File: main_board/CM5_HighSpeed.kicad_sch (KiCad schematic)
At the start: 13 parts, among them J1 USB3_A, J2 USB3_A, J22 690-019-298-412, U12 RT9742SNGV, U6 AP22653W6

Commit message: More power management goodness
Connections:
- net +5v renamed +5V
- net USBOTG_ID: no longer names the net of Module1.101 (USB_OTG_ID)
- no-connect marks 5 -> 35

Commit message: Finalize power management
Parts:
- J1: footprint Library:U3BU1ASMT1 -> 000_custom:U3BU1ASMT1
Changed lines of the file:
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@@
 			)
 		)
-		(property "Footprint" "Library:U3BU1ASMT1"
+		(property "Footprint" "000_custom:U3BU1ASMT1"
 			(at 262.89 40.64 0)
 			(effects

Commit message: Start reouting USB hub
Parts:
- removed J2: USB3_A, Library:U3BU1ASMT1, symbol Connector:USB3_A
- added J8: Conn_01x22_Female, CM5IO:Hirose_FH12-22S-0.5SH_1x22-1MP_P0.50mm_Horizontal, symbol Connector:Conn_01x22_Socket
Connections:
- net USB3-1-D_N renamed USB3_1_DN
- net USB3-1-D_P renamed USB3_1_DP
- net USB3-1-RX_N renamed USB3_1_RX_N
- net USB3-1-RX_P renamed USB3_1_RX_P
- net USB3-1-TX_N renamed USB3_1_TX_N
- net USB3-1-TX_P renamed USB3_1_TX_P

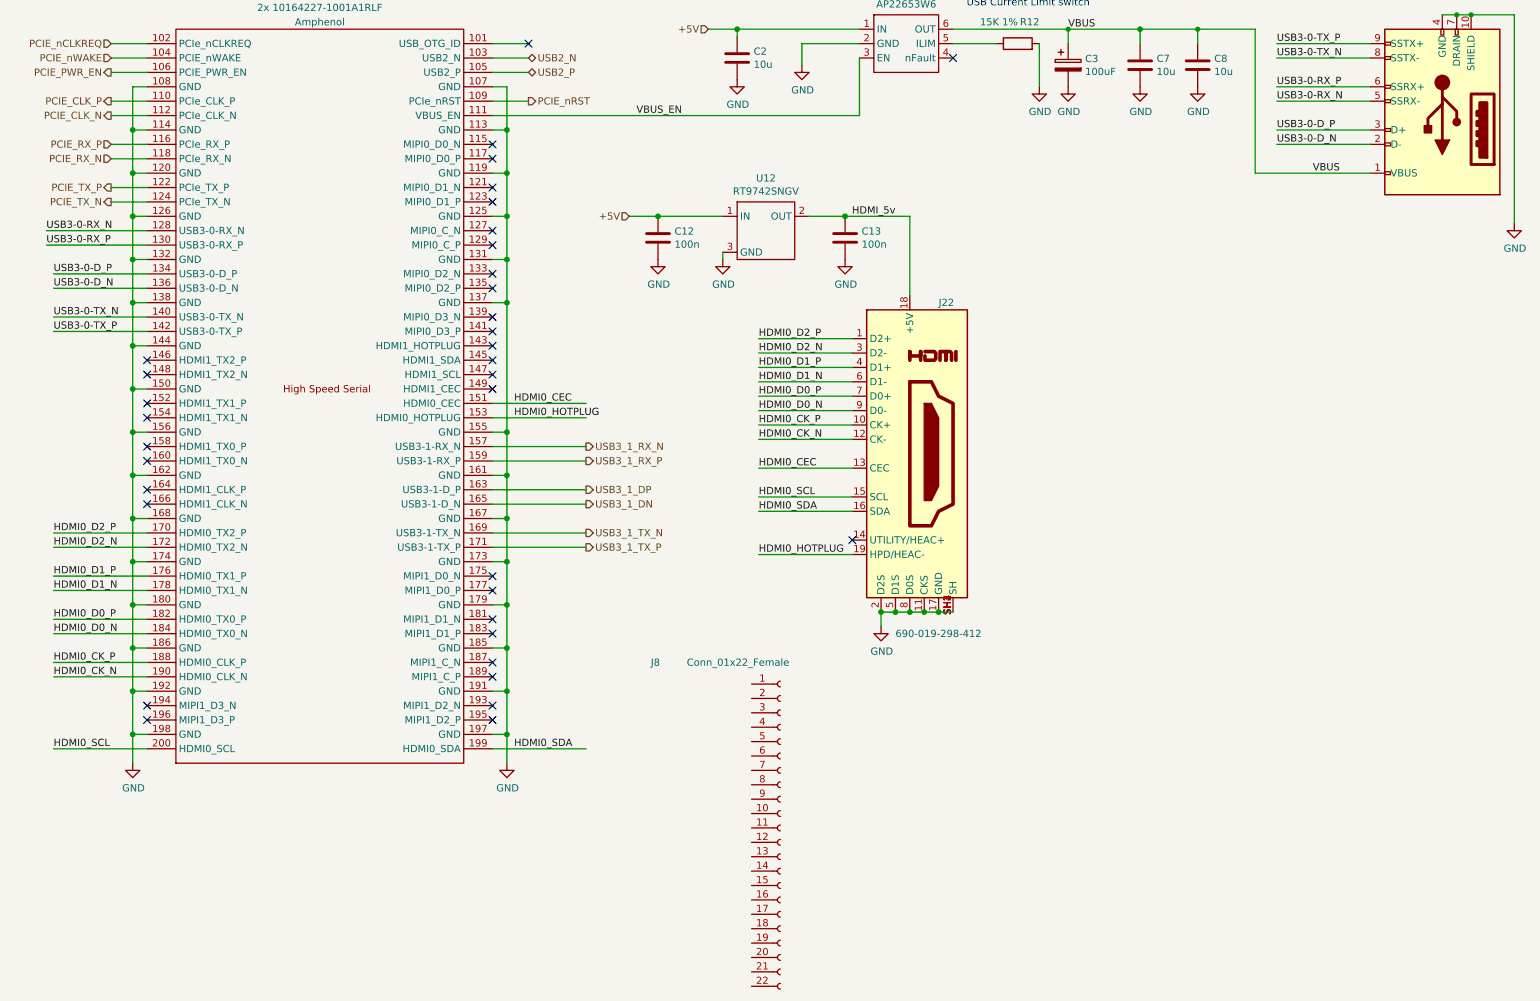
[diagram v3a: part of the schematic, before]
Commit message: Bunch more routing, mainly added MIPI interface, reworked power management a bit
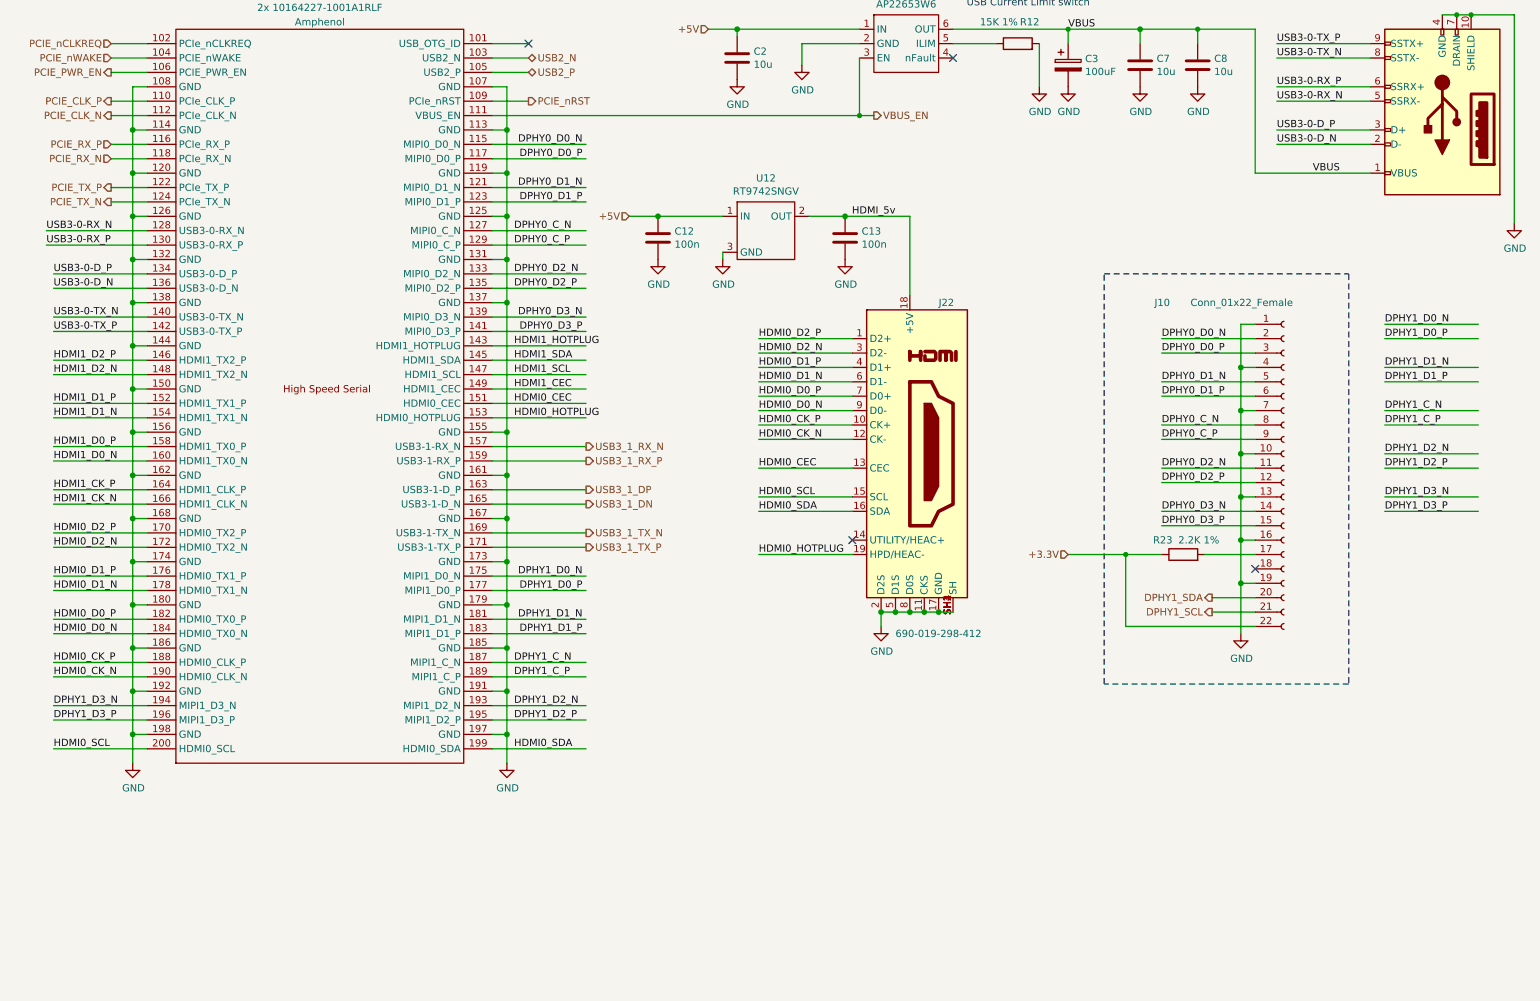
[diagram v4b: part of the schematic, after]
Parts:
- removed J8: Conn_01x22_Female, CM5IO:Hirose_FH12-22S-0.5SH_1x22-1MP_P0.50mm_Horizontal, symbol Connector:Conn_01x22_Socket
- added J10: Conn_01x22_Female, CM5IO:Hirose_FH12-22S-0.5SH_1x22-1MP_P0.50mm_Horizontal, symbol Connector:Conn_01x22_Socket
- added R23: 2.2K 1%, Resistor_SMD:R_0805_2012Metric_Pad1.20x1.40mm_HandSolder, symbol Device:R
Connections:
- net GND: now also J10.1 (Pin_1), J10.10 (Pin_10), J10.13 (Pin_13), J10.16 (Pin_16), J10.19 (Pin_19), J10.4 (Pin_4), J10.7 (Pin_7)
- net DPHY0_D0_N: now reaches Module1.115 (MIPI0_D0_N)
- net DPHY0_D0_N: now also J10.2 (Pin_2)
- net DPHY0_D0_P: now reaches Module1.117 (MIPI0_D0_P)
- net DPHY0_D0_P: now also J10.3 (Pin_3)
- net DPHY0_D1_N: now reaches Module1.121 (MIPI0_D1_N)
- net DPHY0_D1_N: now also J10.5 (Pin_5)
- net DPHY0_D1_P: now reaches Module1.123 (MIPI0_D1_P)
- net DPHY0_D1_P: now also J10.6 (Pin_6)
- net DPHY0_C_N: now reaches Module1.127 (MIPI0_C_N)
- net DPHY0_C_N: now also J10.8 (Pin_8)
- net DPHY0_C_P: now reaches Module1.129 (MIPI0_C_P)
- net DPHY0_C_P: now also J10.9 (Pin_9)
- net DPHY0_D2_N: now reaches Module1.133 (MIPI0_D2_N)
- net DPHY0_D2_N: now also J10.11 (Pin_11)
- net DPHY0_D2_P: now reaches Module1.135 (MIPI0_D2_P)
- net DPHY0_D2_P: now also J10.12 (Pin_12)
- net DPHY0_D3_N: now reaches Module1.139 (MIPI0_D3_N)
- net DPHY0_D3_N: now also J10.14 (Pin_14)
- net DPHY0_D3_P: now reaches Module1.141 (MIPI0_D3_P)
- net DPHY0_D3_P: now also J10.15 (Pin_15)
- net HDMI1_HOTPLUG: now reaches Module1.143 (HDMI1_HOTPLUG)
- net HDMI1_SDA: now reaches Module1.145 (HDMI1_SDA)
- net HDMI1_D2_P: now reaches Module1.146 (HDMI1_TX2_P)
- net HDMI1_SCL: now reaches Module1.147 (HDMI1_SCL)
- net HDMI1_D2_N: now reaches Module1.148 (HDMI1_TX2_N)
- net HDMI1_CEC: now reaches Module1.149 (HDMI1_CEC)
- net HDMI1_D1_P: now reaches Module1.152 (HDMI1_TX1_P)
- net HDMI1_D1_N: now reaches Module1.154 (HDMI1_TX1_N)
- net HDMI1_D0_P: now reaches Module1.158 (HDMI1_TX0_P)
- net HDMI1_D0_N: now reaches Module1.160 (HDMI1_TX0_N)
- net HDMI1_CK_P: now reaches Module1.164 (HDMI1_CLK_P)
- net HDMI1_CK_N: now reaches Module1.166 (HDMI1_CLK_N)
- net DPHY1_D0_N: now reaches Module1.175 (MIPI1_D0_N)
- net DPHY1_D0_P: now reaches Module1.177 (MIPI1_D0_P)
- net DPHY1_D1_N: now reaches Module1.181 (MIPI1_D1_N)
- net DPHY1_D1_P: now reaches Module1.183 (MIPI1_D1_P)
- net DPHY1_C_N: now reaches Module1.187 (MIPI1_C_N)
- net DPHY1_C_P: now reaches Module1.189 (MIPI1_C_P)
- net DPHY1_D2_N: now reaches Module1.193 (MIPI1_D2_N)
- net DPHY1_D3_N: now reaches Module1.194 (MIPI1_D3_N)
- net DPHY1_D2_P: now reaches Module1.195 (MIPI1_D2_P)
- net DPHY1_D3_P: now reaches Module1.196 (MIPI1_D3_P)
- new net: J10.17 (Pin_17), R23.2
- new net +3.3V: J10.22 (Pin_22), R23.1
- new net DPHY1_SCL: J10.21 (Pin_21)
- new net DPHY1_SDA: J10.20 (Pin_20)
- no-connect marks 35 -> 4

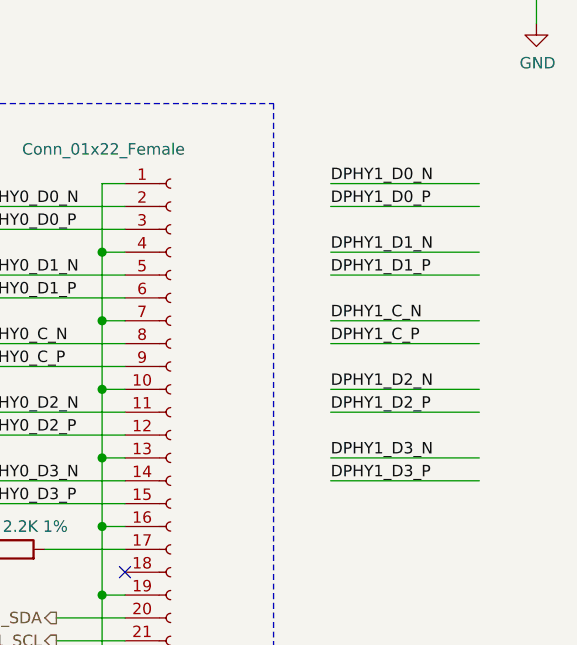
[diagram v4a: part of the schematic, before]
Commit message: Implement power monitoring
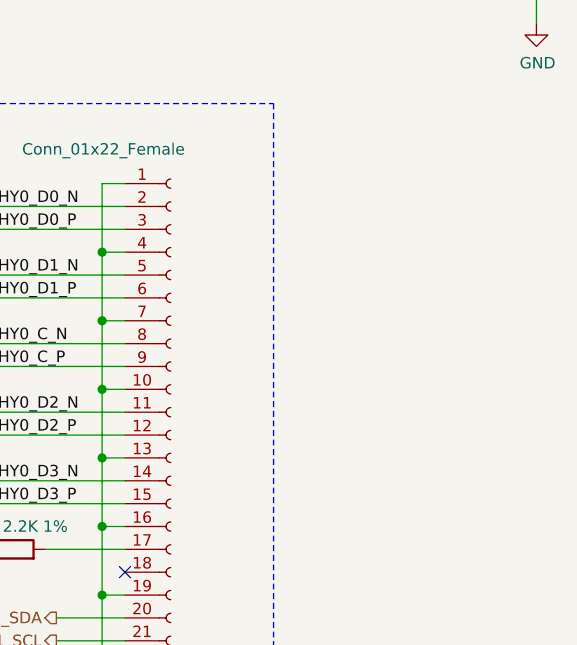
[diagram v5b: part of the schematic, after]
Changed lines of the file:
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@@
-	(wire
-		(pts
-			(xy 256.54 82.55) (xy 273.05 82.55)
-		)
-		(stroke
-			(width 0)
-			(type solid)
-		)
-	)
 	(wire
 		(pts
@@
 	(wire
 		(pts
-			(xy 256.54 92.71) (xy 273.05 92.71)
-		)
-		(stroke
-			(width 0)
-			(type solid)
-		)
-	)
-	(wire
-		(pts
-			(xy 256.54 77.47) (xy 273.05 77.47)
-		)
-		(stroke
-			(width 0)
-			(type solid)
-		)
-	)
-	(wire
-		(pts
 			(xy 99.06 91.44) (xy 115.57 91.44)
 		)
@@
 	(wire
 		(pts
-			(xy 256.54 105.41) (xy 273.05 105.41)
-		)
-		(stroke
-			(width 0)
-			(type solid)
-		)
-	)
-	(wire
-		(pts
 			(xy 233.68 48.26) (xy 254 48.26)
 		)
@@
 	(wire
 		(pts
-			(xy 256.54 97.79) (xy 273.05 97.79)
-		)
-		(stroke
-			(width 0)
-			(type solid)
-		)
-	)
-	(wire
-		(pts
 			(xy 35.56 71.12) (xy 38.1 71.12)
 		)
@@
 	(wire
 		(pts
-			(xy 256.54 85.09) (xy 273.05 85.09)
-		)
-		(stroke
-			(width 0)
-			(type solid)
-		)
-	)
-	(wire
-		(pts
 			(xy 167.64 125.73) (xy 170.18 125.73)
 		)
@@
 		)
 	)
-	(wire
-		(pts
-			(xy 256.54 90.17) (xy 273.05 90.17)
-		)
-		(stroke
-			(width 0)
-			(type solid)
-		)
-	)
 	(polyline
 		(pts
@@
 	(wire
 		(pts
-			(xy 256.54 100.33) (xy 273.05 100.33)
-		)
-		(stroke
-			(width 0)
-			(type solid)
-		)
-	)
-	(wire
-		(pts
 			(xy 101.6 71.12) (xy 101.6 93.98)
 		)
@@
 		(pts
 			(xy 99.06 134.62) (xy 115.57 134.62)
-		)
-		(stroke
-			(width 0)
-			(type solid)
-		)
-	)
-	(wire
-		(pts
-			(xy 256.54 107.95) (xy 273.05 107.95)
-		)
-		(stroke
-			(width 0)
-			(type solid)
-		)
-	)
-	(wire
-		(pts
-			(xy 256.54 74.93) (xy 273.05 74.93)
 		)
 		(stroke
@@
 		)
 	)
-	(label "DPHY1_D2_P"
-		(at 256.54 100.33 0)
-		(fields_autoplaced yes)
-		(effects
-			(font
-				(size 1.27 1.27)
-			)
-			(justify left bottom)
-		)
-	)
 	(label "USB3-0-RX_N"
 		(at 237.49 35.56 0)
@@
 		)
 	)
-	(label "DPHY1_D0_N"
-		(at 256.54 74.93 0)
-		(fields_autoplaced yes)
-		(effects
-			(font
-				(size 1.27 1.27)
-			)
-			(justify left bottom)
-		)
-	)
 	(label "HDMI0_D1_N"
 		(at 146.05 85.09 0)
@@
 		)
 	)
-	(label "DPHY1_D1_P"
-		(at 256.54 85.09 0)
-		(fields_autoplaced yes)
-		(effects
-			(font
-				(size 1.27 1.27)
-			)
-			(justify left bottom)
-		)
-	)
 	(label "DPHY1_C_N"
 		(at 102.87 134.62 0)
@@
 		)
 	)
-	(label "DPHY1_D2_N"
-		(at 256.54 97.79 0)
-		(fields_autoplaced yes)
-		(effects
-			(font
-				(size 1.27 1.27)
-			)
-			(justify left bottom)
-		)
-	)
 	(label "DPHY0_D3_P"
 		(at 217.17 110.49 0)
@@
 		)
 	)
-	(label "DPHY1_D3_N"
-		(at 256.54 105.41 0)
-		(fields_autoplaced yes)
-		(effects
-			(font
-				(size 1.27 1.27)
-			)
-			(justify left bottom)
-		)
-	)
 	(label "USB3-0-D_P"
 		(at 237.49 40.64 0)
@@
 		)
 	)
-	(label "DPHY1_D0_P"
-		(at 256.54 77.47 0)
-		(fields_autoplaced yes)
-		(effects
-			(font
-				(size 1.27 1.27)
-			)
-			(justify left bottom)
-		)
-	)
-	(label "DPHY1_D1_N"
-		(at 256.54 82.55 0)
-		(fields_autoplaced yes)
-		(effects
-			(font
-				(size 1.27 1.27)
-			)
-			(justify left bottom)
-		)
-	)
 	(label "HDMI0_HOTPLUG"
 		(at 102.87 91.44 0)
@@
 		)
 	)
-	(label "DPHY1_D3_P"
-		(at 256.54 107.95 0)
-		(fields_autoplaced yes)
-		(effects
-			(font
-				(size 1.27 1.27)
-			)
-			(justify left bottom)
-		)
-	)
 	(label "HDMI0_CEC"
 		(at 146.05 100.33 0)
@@
 		)
 	)
-	(label "DPHY1_C_P"
-		(at 256.54 92.71 0)
-		(fields_autoplaced yes)
-		(effects
-			(font
-				(size 1.27 1.27)
-			)
-			(justify left bottom)
-		)
-	)
 	(label "DPHY1_D2_P"
 		(at 102.87 144.78 0)
@@
 		(fields_autoplaced yes)
 		(effects
-			(font
-				(size 1.27 1.27)
-			)
-			(justify left bottom)
-		)
-	)
-	(label "DPHY1_C_N"
-		(at 256.54 90.17 0)
-		(fields_autoplaced yes)
-		(effects

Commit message: Rev 1 draft
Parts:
- removed R23: 2.2K 1%, Resistor_SMD:R_0805_2012Metric_Pad1.20x1.40mm_HandSolder, symbol Device:R
- added J11: 501568-0607-TR325, CONN_501568-0607-TR325_MOL, symbol 000_Custom:501568-0607-TR325
- added J12: SM04B-XSRS-ETBLFSN, 000_custom:CONN_SM04B-XSRS-ETB_JST, symbol 000_Custom:SM04B-XSRS-ETBLFSN
- added J13: SM10B-XSRS-ETB, 000_custom:CONN_SM10B-XSRS-ETB_JST, symbol 000_Custom:SM10B-XSRS-ETB
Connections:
- net +3.3V: now also J10.17 (Pin_17); no longer J10.22 (Pin_22)
- net +5V: now also J10.20 (Pin_20), J10.21 (Pin_21), J10.22 (Pin_22), J11.1
- net DPHY0_C_N: now also J10.9 (Pin_9); no longer J10.8 (Pin_8)
- net DPHY0_C_P: now also J10.8 (Pin_8); no longer J10.9 (Pin_9)
- net DPHY0_D0_N: now also J10.15 (Pin_15); no longer J10.2 (Pin_2)
- net DPHY0_D0_P: now also J10.14 (Pin_14); no longer J10.3 (Pin_3)
- net DPHY0_D1_N: now also J10.12 (Pin_12); no longer J10.5 (Pin_5)
- net DPHY0_D1_P: now also J10.11 (Pin_11); no longer J10.6 (Pin_6)
- net DPHY0_D2_N: now also J10.6 (Pin_6); no longer J10.11 (Pin_11)
- net DPHY0_D2_P: now also J10.5 (Pin_5); no longer J10.12 (Pin_12)
- net DPHY0_D3_N: now also J10.3 (Pin_3); no longer J10.14 (Pin_14)
- net DPHY0_D3_P: now also J10.2 (Pin_2); no longer J10.15 (Pin_15)
- net DPHY1_SCL: now also J10.19 (Pin_19); no longer J10.21 (Pin_21)
- net DPHY1_SDA: now also J10.18 (Pin_18); no longer J10.20 (Pin_20)
- net GND: now also R12.1, J11.6, J13.1, J13.2; no longer J10.19 (Pin_19), R12.2
- net HDMI1_CEC: now also J12.4
- net HDMI1_CK_N: now also J13.10
- net HDMI1_CK_P: now also J13.9
- net HDMI1_D0_N: now also J13.8
- net HDMI1_D0_P: now also J13.7
- net HDMI1_D1_N: now also J13.6
- net HDMI1_D1_P: now also J13.5
- net HDMI1_D2_N: now also J13.4
- net HDMI1_D2_P: now also J13.3
- net HDMI1_HOTPLUG: now also J12.1
- net HDMI1_SCL: now also J12.3
- net HDMI1_SDA: now also J12.2
- net at U6.5 (ILIM): now also R12.2; no longer R12.1
- net USB2_N: no longer names the net of Module1.103 (USB2_N)
- net USB2_N: now also J11.2
- net USB2_P: no longer names the net of Module1.105 (USB2_P)
- net USB2_P: now also J11.3
- new net KB_SCL: J11.5
- new net KB_SDA: J11.4
- no-connect marks 4 -> 3
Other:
- moved on the sheet: C12, C13, C2, C3, C7, C8, J10, J22, R12, U12, U6
